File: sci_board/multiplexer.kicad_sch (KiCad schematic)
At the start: 26 parts, among them U13 74LVC3G04, U14 TMUX131RMGR, U15 TMUX131RMGR, U16 74LVC1G139, U17 TMUX131RMGR, U18 TMUX131RMGR, U19 TMUX131RMGR, U20 TMUX131RMGR, U21 TMUX131RMGR, U22 TMUX131RMGR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

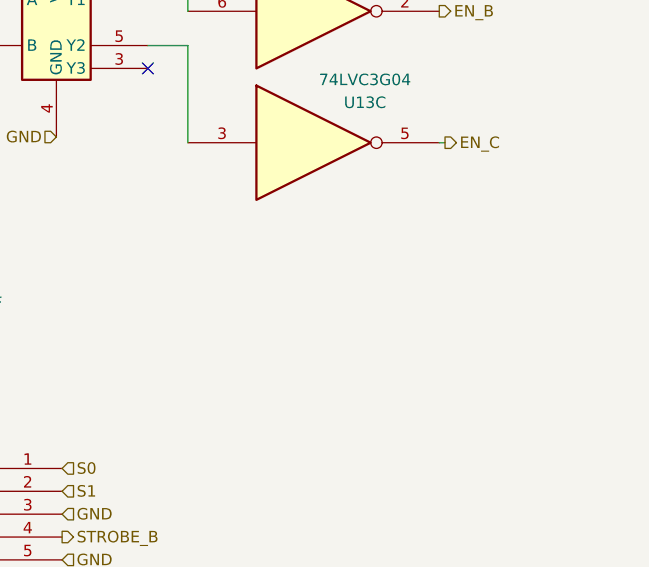
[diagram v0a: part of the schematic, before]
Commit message: clenup BOM for SCI and AUX
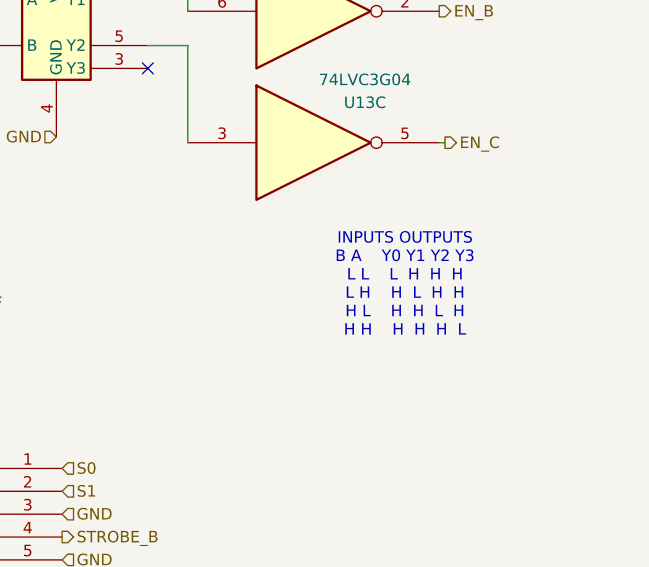
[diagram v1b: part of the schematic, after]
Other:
- note added: "INPUTS OUTPUTS B A Y0 Y1 Y2 Y3 L L L H H H L H H L H H H L H H L H H H H H H L"
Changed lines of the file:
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@@
+		)
+	)
+	(text "INPUTS OUTPUTS\nB A    Y0 Y1 Y2 Y3\nL L    L  H  H  H\nL H    H  L  H  H\nH L    H  H  L  H\nH H    H  H  H  L"
+		(exclude_from_sim no)
+		(at 261.62 104.14 0)
+		(effects
+			(font
+				(size 1.27 1.27)
+			)
 		)
 	)

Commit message: cleaning up bom: remove main camera port since it has not pullups and capacitors, correcting some errors in camera switch
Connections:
- net EN_A: now also U13.5; no longer U13.7
- net EN_B: now also U13.7; no longer U13.2
- net EN_C: now also U13.2; no longer U13.5
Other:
- note added: "S1 S0 OUTPUTS NOUTPUT B A Y0 Y1 Y2 Y3 X0 X1 X2 X3 L L L H H H H L L L L H H L H H L H L L H L H H L H L L H L H H H H H L L L L H"
- note added: "S1 S0 SWITCH STATUS L L D1/D2 connected to S1B/S2B L H D1/D2 connected to S1C/S2C H L D1/D2 connected to S1A/S2A H H All switches in High-Z"
- note removed: "INPUTS OUTPUTS B A Y0 Y1 Y2 Y3 L L L H H H L H H L H H H L H H L H H H H H H L"

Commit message: tweaks before merge
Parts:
- U14, U15, U17, U18, U19, U20, U21, U22, U23: footprint Project:VQFN12_RMG_TEX -> Common:VQFN12_RMG_TEX
